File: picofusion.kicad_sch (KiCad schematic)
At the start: 39 parts, among them J1 NORTH, J2 EAST, J3 WEST, J4 SOUTH, U1 W25Q16, U2 RP2040, U3 TLV71333PDQNT, U7 MCP2544FD, Y1 12MHz

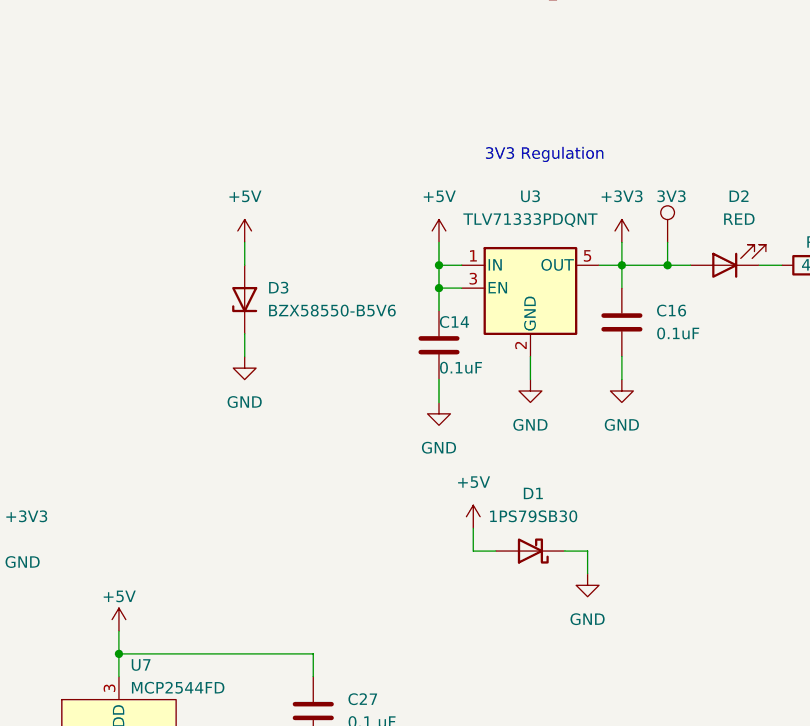
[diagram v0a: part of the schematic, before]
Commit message: schematic: update power protection diode wiring
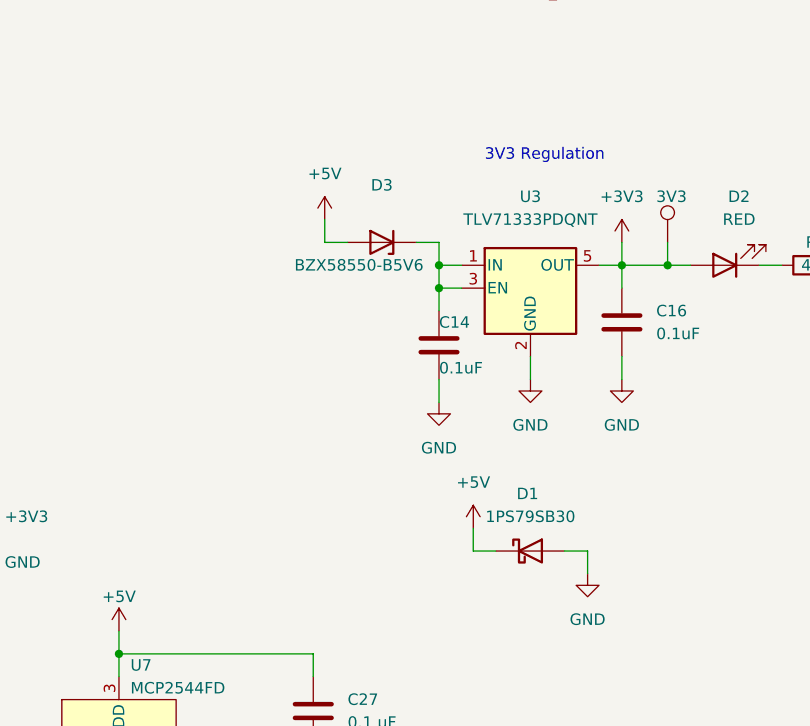
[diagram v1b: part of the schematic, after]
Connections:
- net +5V: now also D1.1 (K); no longer C14.1, D1.2 (A), U3.1 (IN), U3.3 (EN)
- net GND: now also D1.2 (A); no longer D1.1 (K), D3.1 (K)
- new net: C14.1, D3.1 (K), U3.1 (IN), U3.3 (EN)
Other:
- moved on the sheet: D1, D3
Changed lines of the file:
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@@
+    (stroke (width 0) (type default) (color 0 0 0 0))
+  )
+  (wire (pts (xy 176.53 82.55) (xy 179.07 82.55))
     (stroke (width 0) (type default) (color 0 0 0 0))
   )
@@
     (stroke (width 0) (type default) (color 0 0 0 0))
   )
+  (wire (pts (xy 166.37 80.01) (xy 166.37 82.55))
+    (stroke (width 0) (type default) (color 0 0 0 0))
+  )
   (wire (pts (xy 114.3 34.29) (xy 114.3 36.83))
     (stroke (width 0) (type default) (color 0 0 0 0))
@@
     (stroke (width 0) (type solid) (color 0 0 0 0))
   )
+  (wire (pts (xy 166.37 82.55) (xy 168.91 82.55))
+    (stroke (width 0) (type default) (color 0 0 0 0))
+  )
   (wire (pts (xy 91.44 24.13) (xy 99.06 24.13))
     (stroke (width 0) (type solid) (color 0 0 0 0))
@@
     (stroke (width 0) (type solid) (color 0 0 0 0))
   )
-  (wire (pts (xy 157.48 92.71) (xy 157.48 95.25))
-    (stroke (width 0) (type default) (color 0 0 0 0))
-  )
   (wire (pts (xy 52.07 36.83) (xy 52.07 24.13))
     (stroke (width 0) (type solid) (color 0 0 0 0))
@@
   )
   (wire (pts (xy 162.56 35.56) (xy 175.26 35.56))
-    (stroke (width 0) (type default) (color 0 0 0 0))
-  )
-  (wire (pts (xy 157.48 82.55) (xy 157.48 85.09))
     (stroke (width 0) (type default) (color 0 0 0 0))
   )
@@
     (pin "2")
   )
-  (symbol (lib_id "power:+5V") (at 157.48 82.55 0) (unit 1)
-    (in_bom yes) (on_board yes) (fields_autoplaced)
-    (property "Reference" "#PWR0103" (id 0) (at 157.48 86.36 0)
-      (effects (font (size 1.27 1.27)) hide)
-    )
-    (property "Value" "+5V" (id 1) (at 157.48 77.47 0))
-    (property "Footprint" "" (id 2) (at 157.48 82.55 0)
-      (effects (font (size 1.27 1.27)) hide)
-    )
-    (property "Datasheet" "" (id 3) (at 157.48 82.55 0)
-      (effects (font (size 1.27 1.27)) hide)
-    )
-    (pin "1")
-  )
   (symbol (lib_id "power:+1V1") (at 16.51 21.59 0) (unit 1)
     (in_bom yes) (on_board yes) (fields_autoplaced)
@@
     )
     (property "Datasheet" "" (id 3) (at 214.63 149.86 0)
-      (effects (font (size 1.27 1.27)) hide)
-    )
-    (pin "1")
-  )
-  (symbol (lib_id "power:GND") (at 157.48 95.25 0) (unit 1)
-    (in_bom yes) (on_board yes) (fields_autoplaced)
-    (property "Reference" "#PWR0104" (id 0) (at 157.48 101.6 0)
-      (effects (font (size 1.27 1.27)) hide)
-    )
-    (property "Value" "GND" (id 1) (at 157.48 100.33 0))
-    (property "Footprint" "" (id 2) (at 157.48 95.25 0)
-      (effects (font (size 1.27 1.27)) hide)
-    )
-    (property "Datasheet" "" (id 3) (at 157.48 95.25 0)
       (effects (font (size 1.27 1.27)) hide)
     )
@@
     (pin "2")
   )
-  (symbol (lib_id "power:+5V") (at 179.07 82.55 0) (unit 1)
-    (in_bom yes) (on_board yes) (fields_autoplaced)
-    (property "Reference" "#PWR018" (id 0) (at 179.07 86.36 0)
-      (effects (font (size 1.27 1.27)) hide)
-    )
-    (property "Value" "+5V" (id 1) (at 179.07 77.47 0))
-    (property "Footprint" "" (id 2) (at 179.07 82.55 0)
-      (effects (font (size 1.27 1.27)) hide)
-    )
-    (property "Datasheet" "" (id 3) (at 179.07 82.55 0)
+  (symbol (lib_id "power:+5V") (at 166.37 80.01 0) (unit 1)
+    (in_bom yes) (on_board yes) (fields_autoplaced)
+    (property "Reference" "#PWR018" (id 0) (at 166.37 83.82 0)
+      (effects (font (size 1.27 1.27)) hide)
+    )
+    (property "Value" "+5V" (id 1) (at 166.37 74.93 0))
+    (property "Footprint" "" (id 2) (at 166.37 80.01 0)
+      (effects (font (size 1.27 1.27)) hide)
+    )
+    (property "Datasheet" "" (id 3) (at 166.37 80.01 0)
       (effects (font (size 1.27 1.27)) hide)
     )
@@
     (pin "2")
   )
-  (symbol (lib_id "Device:D_Schottky") (at 189.23 116.84 180) (unit 1)
-    (in_bom yes) (on_board yes) (fields_autoplaced)
-    (property "Reference" "D1" (id 0) (at 189.5475 110.49 0))
-    (property "Value" "1PS79SB30" (id 1) (at 189.5475 113.03 0))
+  (symbol (lib_id "Device:D_Schottky") (at 189.23 116.84 0) (unit 1)
+    (in_bom yes) (on_board yes)
+    (property "Reference" "D1" (id 0) (at 188.9125 110.49 0))
+    (property "Value" "1PS79SB30" (id 1) (at 189.23 113.03 0))
     (property "Footprint" "Diode_SMD:D_SOD-523" (id 2) (at 189.23 116.84 0)
       (effects (font (size 1.27 1.27)) hide)
@@
     (pin "2")
   )
-  (symbol (lib_id "Device:D_Zener") (at 157.48 88.9 90) (unit 1)
-    (in_bom yes) (on_board yes) (fields_autoplaced)
-    (property "Reference" "D3" (id 0) (at 160.02 87.6299 90)
-      (effects (font (size 1.27 1.27)) (justify right))
-    )
-    (property "Value" "BZX58550-B5V6" (id 1) (at 160.02 90.1699 90)
-      (effects (font (size 1.27 1.27)) (justify right))
-    )
-    (property "Footprint" "Diode_SMD:D_SOD-523" (id 2) (at 157.48 88.9 0)
-      (effects (font (size 1.27 1.27)) hide)
-    )
-    (property "Datasheet" "~" (id 3) (at 157.48 88.9 0)
+  (symbol (lib_id "Device:D_Zener") (at 172.72 82.55 180) (unit 1)
+    (in_bom yes) (on_board yes)
+    (property "Reference" "D3" (id 0) (at 172.72 76.2 0))
+    (property "Value" "BZX58550-B5V6" (id 1) (at 170.18 85.09 0))
+    (property "Footprint" "Diode_SMD:D_SOD-523" (id 2) (at 172.72 82.55 0)
+      (effects (font (size 1.27 1.27)) hide)
+    )
+    (property "Datasheet" "~" (id 3) (at 172.72 82.55 0)
       (effects (font (size 1.27 1.27)) hide)
     )
@@
       (reference "#PWR0102") (unit 1) (value "GND") (footprint "")
     )
-    (path "/0f1b439c-d8ea-4fd9-a1a6-dac6d808b050"
-      (reference "#PWR0103") (unit 1) (value "+5V") (footprint "")
-    )
-    (path "/176e2ba3-54f3-44c0-8b9f-37384f9980b9"
-      (reference "#PWR0104") (unit 1) (value "GND") (footprint "")
-    )
     (path "/c9c10321-e8b2-453c-8e2a-7fc3d38ad8ba"

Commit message: routing cleanup, merge minor schematic fixes
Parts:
- C11, C14, C16, C27: LCSC (none) -> C1525
- C15, C24, C26: LCSC C52923 -> C1525
- C5, C8: LCSC (none) -> C1547
- D1: LCSC (none) -> C426690
- D2: value RED -> GREEN; LCSC (none) -> C72043
- R1, R4, R5: LCSC (none) -> C25744
- R6: LCSC (none) -> C25117
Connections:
- net SPI1_PICO_SD: now also J2.3 (Pin_3); no longer J2.4 (Pin_4)
- net SPI1_POCI_SD: now also J2.2 (Pin_2); no longer J2.1 (Pin_1)
- net SPI1_SCK_SD: now also J2.1 (Pin_1); no longer J2.3 (Pin_3)
- net SPI1_nCS_SD: now also J2.4 (Pin_4); no longer J2.2 (Pin_2)
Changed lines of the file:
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@@
     (effects (font (size 1.27 1.27)) (justify right bottom))
   )
-  (label "SPI1_SCK_SD" (at 247.65 69.85 0)
+  (label "SPI1_SCK_SD" (at 247.65 64.77 0)
     (effects (font (size 1.27 1.27)) (justify left bottom))
   )
@@
     (effects (font (size 1.27 1.27)) (justify left bottom))
   )
-  (label "SPI1_POCI_SD" (at 247.65 64.77 0)
+  (label "SPI1_POCI_SD" (at 247.65 67.31 0)
     (effects (font (size 1.27 1.27)) (justify left bottom))
   )
@@
     (effects (font (size 1.27 1.27)) (justify right bottom))
   )
-  (label "SPI1_PICO_SD" (at 247.65 72.39 0)
+  (label "SPI1_PICO_SD" (at 247.65 69.85 0)
     (effects (font (size 1.27 1.27)) (justify left bottom))
   )
@@
     (effects (font (size 1.27 1.27)) (justify right bottom))
   )
-  (label "SPI1_nCS_SD" (at 247.65 67.31 0)
+  (label "SPI1_nCS_SD" (at 247.65 72.39 0)
     (effects (font (size 1.27 1.27)) (justify left bottom))
   )
@@
       (effects (font (size 1.27 1.27)) hide)
     )
+    (property "LCSC" "C1525" (id 4) (at 107.95 176.53 0)
+      (effects (font (size 1.27 1.27)) hide)
+    )
     (pin "1")
     (pin "2")
@@
       (effects (font (size 1.27 1.27)) hide)
     )
-    (property "LCSC" "C52923" (id 4) (at 121.92 30.48 0)
+    (property "LCSC" "C1525" (id 4) (at 121.92 30.48 0)
       (effects (font (size 1.27 1.27)) hide)
     )
@@
       (effects (font (size 1.27 1.27)) hide)
     )
-    (property "LCSC" "" (id 4) (at 91.44 176.53 0)
+    (property "LCSC" "C1547" (id 4) (at 91.44 176.53 0)
       (effects (font (size 1.27 1.27)) hide)
     )
@@
     )
     (property "Datasheet" "~" (id 3) (at 199.39 91.44 0)
+      (effects (font (size 1.27 1.27)) hide)
+    )
+    (property "LCSC" "C1525" (id 4) (at 199.39 91.44 0)
       (effects (font (size 1.27 1.27)) hide)
     )
@@
       (effects (font (size 1.27 1.27)) hide)
     )
-    (property "LCSC" "" (id 4) (at 78.74 176.53 0)
+    (property "LCSC" "C1547" (id 4) (at 78.74 176.53 0)
       (effects (font (size 1.27 1.27)) hide)
     )
@@
       (effects (font (size 1.27 1.27)) hide)
     )
-    (property "LCSC" "C52923" (id 4) (at 129.54 30.48 0)
+    (property "LCSC" "C1525" (id 4) (at 129.54 30.48 0)
       (effects (font (size 1.27 1.27)) hide)
     )
@@
       (effects (font (size 1.27 1.27)) hide)
     )
-    (property "LCSC" "C52923" (id 4) (at 137.16 30.48 0)
+    (property "LCSC" "C1525" (id 4) (at 137.16 30.48 0)
       (effects (font (size 1.27 1.27)) hide)
     )
@@
     )
     (property "Datasheet" "~" (id 3) (at 120.65 113.03 0)
+      (effects (font (size 1.27 1.27)) hide)
+    )
+    (property "LCSC" "C25744" (id 4) (at 120.65 113.03 0)
       (effects (font (size 1.27 1.27)) hide)
     )
@@
       (effects (font (size 1.27 1.27)) hide)
     )
+    (property "LCSC" "C1525" (id 4) (at 179.07 93.98 0)
+      (effects (font (size 1.27 1.27)) hide)
+    )
     (pin "1")
     (pin "2")
@@
       (effects (font (size 1.27 1.27)) hide)
     )
+    (property "LCSC" "C25744" (id 4) (at 107.95 163.83 0)
+      (effects (font (size 1.27 1.27)) hide)
+    )
     (pin "1")
     (pin "2")
@@
       (effects (font (size 1.27 1.27)) hide)
     )
+    (property "LCSC" "C426690" (id 4) (at 189.23 116.84 0)
+      (effects (font (size 1.27 1.27)) hide)
+    )
     (pin "1")
     (pin "2")
@@
     )
     (property "Datasheet" "~" (id 3) (at 220.98 85.09 0)
+      (effects (font (size 1.27 1.27)) hide)
+    )
+    (property "LCSC" "C25117" (id 4) (at 220.98 85.09 0)
       (effects (font (size 1.27 1.27)) hide)
     )
@@
       (effects (font (size 1.27 1.27)) hide)
     )
+    (property "LCSC" "C1525" (id 4) (at 165.1 134.62 0)
+      (effects (font (size 1.27 1.27)) hide)
+    )
     (pin "1")
     (pin "2")
@@
     (in_bom yes) (on_board yes)
     (property "Reference" "D2" (id 0) (at 212.4075 77.47 0))
-    (property "Value" "RED" (id 1) (at 212.4075 80.01 0))
+    (property "Value" "GREEN" (id 1) (at 212.4075 80.01 0))
     (property "Footprint" "LED_SMD:LED_0402_1005Metric" (id 2) (at 210.82 85.09 0)
       (effects (font (size 1.27 1.27)) hide)
     )
     (property "Datasheet" "~" (id 3) (at 210.82 85.09 0)
+      (effects (font (size 1.27 1.27)) hide)
+    )
+    (property "LCSC" "C72043" (id 4) (at 210.82 85.09 0)
       (effects (font (size 1.27 1.27)) hide)
     )
@@
     )
     (property "Datasheet" "~" (id 3) (at 120.65 118.11 0)
+      (effects (font (size 1.27 1.27)) hide)
+    )
+    (property "LCSC" "C25744" (id 4) (at 120.65 118.11 0)
       (effects (font (size 1.27 1.27)) hide)
     )
@@
     )
     (path "/e7c8b4ea-aa55-4149-b049-80dac4f474a9"
-      (reference "D2") (unit 1) (value "RED") (footprint "LED_SMD:LED_0402_1005Metric")
+      (reference "D2") (unit 1) (value "GREEN") (footprint "LED_SMD:LED_0402_1005Metric")
     )
     (path "/d8ec1a54-37bc-4303-a25d-edfa5fb66a21"
@@
     )
     (path "/1053d281-834b-4710-be99-168959d6bce0/004c481e-af69-4b39-b35d-a9942872116f"
-      (reference "R8") (unit 1) (value "2.7K") (footprint "Resistor_SMD:R_0402_1005Metric")
+      (reference "R8") (unit 1) (value "1.5K") (footprint "Resistor_SMD:R_0402_1005Metric")
     )
     (path "/1053d281-834b-4710-be99-168959d6bce0/778bd863-ba55-4ebd-8e98-3e8cd6b1235a"
-      (reference "R9") (unit 1) (value "2.7K") (footprint "Resistor_SMD:R_0402_1005Metric")
+      (reference "R9") (unit 1) (value "1.5K") (footprint "Resistor_SMD:R_0402_1005Metric")
     )
     (path "/5e5fc09c-a533-4248-937c-15ae2153c06c"
       (reference "TP1") (unit 1) (value "QSPI_SCK") (footprint "TestPoint:TestPoint_Pad_1.0x1.0mm")
     )
+    (path "/1053d281-834b-4710-be99-168959d6bce0/7200cdfe-1dfd-480e-ac25-3225a5f9f7f4"
+      (reference "TP2") (unit 1) (value "TestPoint") (footprint "TestPoint:TestPoint_Pad_1.0x1.0mm")
+    )
+    (path "/1053d281-834b-4710-be99-168959d6bce0/7272ad07-297d-40ad-a749-6b3a12c8110c"
+      (reference "TP3") (unit 1) (value "TestPoint") (footprint "TestPoint:TestPoint_Pad_1.0x1.0mm")
+    )
+    (path "/1053d281-834b-4710-be99-168959d6bce0/4d3d12d9-61ec-4395-a12a-b445bf230008"
+      (reference "TP4") (unit 1) (value "TestPoint") (footprint "TestPoint:TestPoint_Pad_1.0x1.0mm")
+    )
     (path "/2b6f5c8a-05cf-4448-8322-d77121105d11"

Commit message: Replace current transceiver with TJA1051TK/3118 and add work on GND/power routing
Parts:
- removed U7: MCP2544FD, Package_SO:SOP-8_3.9x4.9mm_P1.27mm, symbol mcp2544fd:MCP2544FD
- added C28: 0.1 µF, Capacitor_SMD:C_0402_1005Metric, symbol Device:C
- added R10, R11: 100K, Resistor_SMD:R_0402_1005Metric, symbol Device:R
- added U7: TJA1051TK-3, Package_DFN_QFN:DFN-8-1EP_3x3mm_P0.65mm_EP1.55x2.4mm, symbol Interface_CAN_LIN:TJA1051TK-3
- C27: LCSC C1525 -> (none)
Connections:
- net +3V3: now also C27.1, R11.1, U7.5 (VIO)
- net +5V: now also C28.1, U7.3 (VCC); no longer C27.1
- net CAN_N: now also J3.6 (Pin_6), U7.6 (CANL); no longer J3.7 (Pin_7)
- net CAN_P: now also J3.7 (Pin_7), U7.7 (CANH); no longer J3.6 (Pin_6)
- net GND: now also C28.2, R10.2, U7.2 (GND), U7.9 (GND)
- net PIO0_CAN_RX: now also U7.4 (RXD)
- net PIO0_CAN_TX: now also U7.1 (TXD)
- net CAN_STBY renamed CAN_SILENT
- net CAN_SILENT: now also R10.1, R11.2, U7.8 (S)

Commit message: layout: cleanup, planes, some drc
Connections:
- net CAN_SILENT: now also U2.13 (GPIO10); no longer U2.9 (GPIO7)
- net IMU_HEATER: now also U2.14 (GPIO11); no longer U2.13 (GPIO10)
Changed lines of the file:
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@@
   (no_connect (at 262.89 96.52))
   (no_connect (at 262.89 99.06))
-  (no_connect (at 96.52 82.55))
+  (no_connect (at 96.52 72.39))
   (no_connect (at 96.52 85.09))
   (no_connect (at 96.52 92.71))
@@
     (stroke (width 0) (type solid) (color 0 0 0 0))
   )
-  (wire (pts (xy 96.52 72.39) (xy 114.3 72.39))
+  (wire (pts (xy 96.52 80.01) (xy 114.3 80.01))
     (stroke (width 0) (type default) (color 0 0 0 0))
   )
@@
     (stroke (width 0) (type solid) (color 0 0 0 0))
   )
-  (wire (pts (xy 96.52 80.01) (xy 114.3 80.01))
+  (wire (pts (xy 96.52 82.55) (xy 114.3 82.55))
     (stroke (width 0) (type default) (color 0 0 0 0))
   )
@@
     (effects (font (size 1.27 1.27)) (justify right bottom))
   )
-  (label "IMU_HEATER" (at 114.3 80.01 180)
+  (label "IMU_HEATER" (at 114.3 82.55 180)
     (effects (font (size 1.27 1.27)) (justify right bottom))
   )
@@
     (effects (font (size 1.27 1.27)) (justify left bottom))
   )
-  (label "CAN_SILENT" (at 114.3 72.39 180)
-    (effects (font (size 1.27 1.27)) (justify right bottom))
-  )
+  (label "CAN_SILENT" (at 114.3 80.01 180)
+    (effects (font (size 1.27 1.27)) (justify right bottom))
+  )

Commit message: Finish R01A
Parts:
- removed TP1: QSPI_SCK, TestPoint:TestPoint_Pad_1.0x1.0mm, symbol Connector:TestPoint
- removed U3: TLV71333PDQNT, Package_SON:Texas_X2SON-4_1x1mm_P0.65mm, symbol Regulator_Linear:TLV71333PDBV
- added R12, R13: 0, Resistor_SMD:R_0402_1005Metric, symbol Device:R
- added U3: TLV71333PDQN, Package_SON:Texas_X2SON-4_1x1mm_P0.65mm, symbol TLV71333PDQ:TLV71333PDQN
- C27, C28: value 0.1 µF -> 0.1uF; LCSC (none) -> C1525
- R10, R11: LCSC (none) -> C25741
- R2, R3: LCSC (none) -> C31439
- U1: LCSC C97521 -> C2843335
- U7: LCSC (none) -> C124020
- Y1: LCSC (none) -> C521567
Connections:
- net +3V3: now also U3.1 (OUT)
- net CAN_N: now also R13.2
- net CAN_P: now also R12.2
- net GND: now also U3.2 (GND), U3.5 (GND); no longer J3.4 (Pin_4)
- net NEOPIXEL: now also J3.4 (Pin_4), U2.9 (GPIO7); no longer U2.17 (GPIO14)
- net PIO0_CAN_RX: now also R13.1
- net PIO0_CAN_TX: now also R12.1
- net SPI0_POCI: now also J3.3 (Pin_3)
- net at C14.1, D3.1 (K): now also U3.3 (EN), U3.4 (IN)
- net SDA/SDI: now reaches J3.1 (Pin_1)
- net SCL/SCK: now reaches J3.2 (Pin_2)
- no-connect marks 9 -> 6
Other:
- sheet Sensor Suite ports: added SCL/SCK, SDA/SDI; removed none
- note removed: "TODO: Reorder"

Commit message: Finish R01B
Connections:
- net DRDY_ICM42605 renamed DRDY_ICM20602
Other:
- sheet Sensor Suite ports: added DRDY_ICM20602; removed DRDY_ICM42605
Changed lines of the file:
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@@
     (effects (font (size 1.27 1.27)) (justify left bottom))
   )
-  (label "DRDY_ICM42605" (at 114.3 69.85 180)
+  (label "DRDY_ICM20602" (at 114.3 69.85 180)
     (effects (font (size 1.27 1.27)) (justify right bottom))
   )
@@
     (effects (font (size 1.27 1.27)) (justify left bottom))
   )
-  (label "DRDY_ICM42605" (at 157.48 43.18 0)
+  (label "DRDY_ICM20602" (at 157.48 43.18 0)
     (effects (font (size 1.27 1.27)) (justify left bottom))
   )
@@
       (effects (font (size 1.27 1.27)) (justify left))
     )
-    (pin "DRDY_ICM42605" input (at 175.26 43.18 180)
-      (effects (font (size 1.27 1.27)) (justify left))
-    )
     (pin "nCS" input (at 175.26 40.64 180)
       (effects (font (size 1.27 1.27)) (justify left))
@@
     )
     (pin "SCL{slash}SCK" input (at 175.26 55.88 180)
+      (effects (font (size 1.27 1.27)) (justify left))
+    )
+    (pin "DRDY_ICM20602" input (at 175.26 43.18 180)
       (effects (font (size 1.27 1.27)) (justify left))
     )
@@
       (reference "#PWR029") (unit 1) (value "GND") (footprint "")
     )
-    (path "/1053d281-834b-4710-be99-168959d6bce0/510cd82b-322e-40f0-a643-c99e6ba10850"
-      (reference "#PWR030") (unit 1) (value "GND") (footprint "")
-    )
     (path "/1053d281-834b-4710-be99-168959d6bce0/f4d12da7-fe30-4907-a79d-3b873a478eb9"
       (reference "#PWR031") (unit 1) (value "GND") (footprint "")
     )
-    (path "/1053d281-834b-4710-be99-168959d6bce0/f29f5827-ddff-4593-996d-398b9111b871"
-      (reference "#PWR032") (unit 1) (value "GND") (footprint "")
-    )
     (path "/5a805fd3-f867-47fa-bc15-a0dc21432ce2"
       (reference "#PWR033") (unit 1) (value "GND") (footprint "")
@@
       (reference "#PWR0102") (unit 1) (value "GND") (footprint "")
     )
+    (path "/1053d281-834b-4710-be99-168959d6bce0/188e3eca-ef80-454e-b003-bb93a04b9e44"
+      (reference "#PWR0103") (unit 1) (value "GND") (footprint "")
+    )
+    (path "/1053d281-834b-4710-be99-168959d6bce0/acd764d6-f510-4a64-bdcc-afd6dcc6a24d"
+      (reference "#PWR0104") (unit 1) (value "GND") (footprint "")
+    )
     (path "/c9c10321-e8b2-453c-8e2a-7fc3d38ad8ba"
       (reference "#PWR0105") (unit 1) (value "GND") (footprint "")
@@
       (reference "#PWR0110") (unit 1) (value "+5V") (footprint "")
     )
+    (path "/1053d281-834b-4710-be99-168959d6bce0/2ae7645e-ed80-465e-8121-1b6c78547f38"
+      (reference "#PWR0111") (unit 1) (value "GND") (footprint "")
+    )
     (path "/5f13a28e-82a1-4e85-b4bc-5dfc256ed5f9"
       (reference "3V3") (unit 1) (value "TestPoint") (footprint "TestPoint:TestPoint_Pad_1.0x1.0mm")
@@
       (reference "C28") (unit 1) (value "0.1uF") (footprint "Capacitor_SMD:C_0402_1005Metric")
     )
+    (path "/1053d281-834b-4710-be99-168959d6bce0/0f375347-e816-4f65-9365-deec5a53e7ae"
+      (reference "C29") (unit 1) (value "0.1uF") (footprint "Capacitor_SMD:C_0402_1005Metric")
+    )
     (path "/83435655-435e-44cf-8361-2ea2525423d1"
       (reference "D1") (unit 1) (value "1PS79SB30") (footprint "Diode_SMD:D_SOD-523")
@@
       (reference "U3") (unit 1) (value "TLV71333PDQN") (footprint "Package_SON:Texas_X2SON-4_1x1mm_P0.65mm")
     )
-    (path "/1053d281-834b-4710-be99-168959d6bce0/86fe9ef2-9925-4003-bfa5-7245f7d373ab"
-      (reference "U4") (unit 1) (value "ICM42605") (footprint "Package_LGA:LGA-14_3x2.5mm_P0.5mm_LayoutBorder3x4y")
+    (path "/1053d281-834b-4710-be99-168959d6bce0/a7caa87b-cd5b-4555-b887-52a7ac684483"
+      (reference "U4") (unit 1) (value "ICM-20602") (footprint "Package_LGA:LGA-16_3x3mm_P0.5mm_LayoutBorder3x5y")
     )
     (path "/1053d281-834b-4710-be99-168959d6bce0/af452c33-ef15-4712-8131-5d8dce3be106"

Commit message: more work
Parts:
- added R18, R19, R22: 0, Resistor_SMD:R_0402_1005Metric, symbol Device:R
- added R20: 1K, Resistor_SMD:R_0402_1005Metric, symbol Device:R
- added R21: 10K, Resistor_SMD:R_0402_1005Metric, symbol Device:R
- R10: DNP (none) -> [DNP]
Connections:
- net +3V3: now also R21.1
- net DRDY_ICM20602: now also R22.1
- net GND: now also R18.2, R19.2; no longer J1.4 (Pin_4)
- net NEOPIXEL: now also R22.2
- net RUN: now also R18.1
- net QSPI_SS renamed QSPI_nCS
- net QSPI_nCS: now also R20.2, R21.2
- new net BOOTSEL: J1.4 (Pin_4), R19.1, R20.1
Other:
- note added: "Bridge w/ screwdriver for testing"
- moved on the sheet: C11, R1, R10, R11, R12, R13, U7
